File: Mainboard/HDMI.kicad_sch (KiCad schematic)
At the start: 54 parts, among them J3 HDMI_A, Q1 2N7002, Q2 2SK3018, Q3 2SK3018, Q4 2SK3018, U1 TPAZ1023-04F, U2 TPAZ1023-04F, U6 ADV7613WBBCZ, Y1 SiT8008xx-1x-xxE

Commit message: Added HDMI > LDVS screens
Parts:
- removed C25: 100nF/16V, A_HDJ_Library:C_0402_1005Metric, symbol Device:C
- removed F1: 6V/50mA, A_HDJ_Library:R_0603_1608Metric, symbol Device:Fuse
- removed J3: HDMI_A, A_HDJ_Library:HDMI_A_Molex_208658-1001_Horizontal, symbol Connector:HDMI_A
- renumbered C17 to C25, C18 to C33, C19 to C34, C20 to C35, C21 to C36, C22 to C37, C23 to C38, C24 to C39, D1 to D34, D2 to D35, D3 to D36, D4 to D37, Q2 to Q10, Q3 to Q17, Q4 to Q18, Q1 to Q9, R5 to R104, R6 to R105, R7 to R106, R8 to R107, R9 to R108, R10 to R109, R11 to R110, R12 to R111, R13 to R112, R14 to R113, R15 to R114, R16 to R115, R17 to R116, R18 to R117, R19 to R118, R20 to R119, R21 to R120, R22 to R121, R23 to R122, R24 to R123, R25 to R124, R61 to R125, R62 to R126, R98 to R127, R99 to R128, R100 to R129, R101 to R130, R102 to R131, R103 to R132, R3 to R28, R4 to R76, U6 to U20, U1 to U7, U2 to U8, Y1 to Y2
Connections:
- net +1V8: now also U20.B7 (INT), U20.C3 (CVDD), U20.C6 (DVDD), U20.D3 (CVDD), U20.D6 (DVDD), U20.E3 (CVDD), U20.E6 (DVDD), U20.E7 (DVDD), U20.G1 (CVDD), U20.G2 (CVDD), U20.H2 (LTX_VDD), U20.H3 (LTX_VDD), U20.H6 (LTX_VDD), U20.H7 (LTX_VDD)
- net +3V3: now also U20.F3 (TVDD), U20.F7 (DVDDIO), U20.G3 (TVDD), U20.G7 (DVDDIO)
- net +5V: now also U20.B1 (RXA_5V)
- net DDC_SCL: now also U20.A3 (DDCA_SCL)
- net DDC_SDA: now also U20.A2 (DDCA_SDA)
- net GND: now also U20.A7 (RESET*), U20.B6 (CS*)
- net HPD: now also U20.B2 (HPA_A)
- net TMDS_CK+: now also U20.C1 (RXA_C+)
- net TMDS_CK-: now also U20.C2 (RXA_C-)
- net TMDS_D0+: now also U20.D1 (RXA_0+)
- net TMDS_D0-: now also U20.D2 (RXA_0-)
- net TMDS_D1+: now also U20.E1 (RXA_1+)
- net TMDS_D1-: now also U20.E2 (RXA_1-)
- net TMDS_D2+: now also U20.F1 (RXA_2+)
- net TMDS_D2-: now also U20.F2 (RXA_2-)
- net I2C2_SCL: now reaches U20.A8 (SCL)
- net I2C2_SDA: now reaches U20.B8 (SDA)
- net LTX2_3-: now reaches U20.H1 (LTX2_3-)
- net LTX1_0-: now reaches U20.H10 (LTX1_0-)
- net LTX2_3+: now reaches U20.J1 (LTX2_3+)
- net LTX1_0+: now reaches U20.J10 (LTX1_0+)
- net LTX2_C-: now reaches U20.J2 (LTX2_C-)
- net LTX2_2-: now reaches U20.J3 (LTX2_2-)
- net LTX2_1-: now reaches U20.J4 (LTX2_1-)
- net LTX2_0-: now reaches U20.J5 (LTX2_0-)
- net LTX1_3-: now reaches U20.J6 (LTX1_3-)
- net LTX1_C-: now reaches U20.J7 (LTX1_C-)
- net LTX1_2-: now reaches U20.J8 (LTX1_2-)
- net LTX1_1-: now reaches U20.J9 (LTX1_1-)
- net LTX2_C+: now reaches U20.K2 (LTX2_C+)
- net LTX2_2+: now reaches U20.K3 (LTX2_2+)
- net LTX2_1+: now reaches U20.K4 (LTX2_1+)
- net LTX2_0+: now reaches U20.K5 (LTX2_0+)
- net LTX1_3+: now reaches U20.K6 (LTX1_3+)
- net LTX1_C+: now reaches U20.K7 (LTX1_C+)
- net LTX1_2+: now reaches U20.K8 (LTX1_2+)
- net LTX1_1+: now reaches U20.K9 (LTX1_1+)
- net DDI_B_DDC_SCL renamed TCP_0_DDC_SCL
- net TCP_0_DDC_SCL: no longer U20.A3 (DDCA_SCL)
- net DDI_B_DDC_SDA renamed TCP_0_DDC_SDA
- net TCP_0_DDC_SDA: no longer U20.A2 (DDCA_SDA)
- net DDI_B_HPD renamed TCP_0_HPD
- net TCP_0_HPD: no longer U20.B2 (HPA_A)
- net DDI_B_TX0+ renamed TCP_0_TX0+
- net DDI_B_TX0- renamed TCP_0_TX0-
- net DDI_B_TX1+ renamed TCP_0_TX1+
- net DDI_B_TX1- renamed TCP_0_TX1-
- net DDI_B_TX2+ renamed TCP_0_TX2+
- net DDI_B_TX2- renamed TCP_0_TX2-
- net DDI_B_TX3+ renamed TCP_0_TX3+
- net DDI_B_TX3- renamed TCP_0_TX3-
- no-connect marks 3 -> 10
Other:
- moved on the sheet: C25, C33, C34, C35, C36, C37, C38, C39, D34, D35, D36, D37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

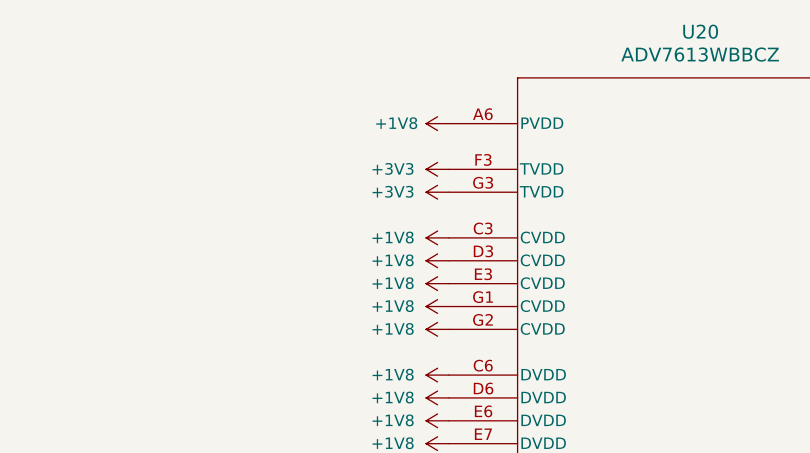
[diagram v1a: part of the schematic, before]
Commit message: Mainboard Progress, Updated CTRL-L for new Joystick Module
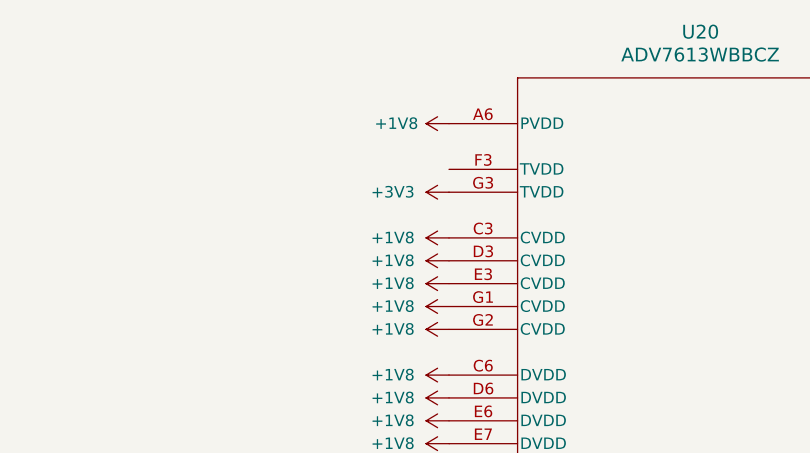
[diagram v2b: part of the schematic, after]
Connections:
- net +3V3: no longer U20.F3 (TVDD)
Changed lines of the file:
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@@
 	)
 	(symbol
-		(lib_name "+5V_1")
-		(lib_id "power:+5V")
-		(at 411.48 212.09 90)
-		(unit 1)
-		(body_style 1)
-		(exclude_from_sim no)
-		(in_bom yes)
-		(on_board yes)
-		(in_pos_files yes)
-		(dnp no)
-		(fields_autoplaced yes)
-		(property "Reference" "#PWR0169"
-			(at 415.29 212.09 0)
-			(hide yes)
-			(show_name no)
-			(do_not_autoplace no)
-			(effects
-				(font
-					(size 1.27 1.27)
-				)
-			)
-		)
-		(property "Value" "+5V"
-			(at 407.67 212.0899 90)
-			(show_name no)
-			(do_not_autoplace no)
-			(effects
-				(font
-					(size 1.27 1.27)
-				)
-				(justify left)
-			)
-		)
-		(property "Footprint" ""
-			(at 411.48 212.09 0)
-			(hide yes)
-			(show_name no)
-			(do_not_autoplace no)
-			(effects
-				(font
-					(size 1.27 1.27)
-				)
-			)
-		)
-		(property "Datasheet" ""
-			(at 411.48 212.09 0)
-			(hide yes)
-			(show_name no)
-			(do_not_autoplace no)
-			(effects
-				(font
-					(size 1.27 1.27)
-				)
-			)
-		)
-		(property "Description" "Power symbol creates a global label with name \"+5V\""
-			(at 411.48 212.09 0)
-			(hide yes)
-			(show_name no)
-			(do_not_autoplace no)
-			(effects
-				(font
-					(size 1.27 1.27)
-				)
-			)
-		)
-		(pin "1"
-		)
-		(instances
-			(project "[DFR1142]Lite Carrier for LattePanda Mu(V2)"
-				(path "/2a6d114a-7fd7-4207-b5f7-4ea9c34f36aa/18101890-54d7-4e46-b21c-77a03deab3c0"
-					(reference "#PWR0169")
-					(unit 1)
-				)
-				(path "/2a6d114a-7fd7-4207-b5f7-4ea9c34f36aa/b169c362-0273-44a3-bb19-0bcbad977976"
-					(reference "#PWR0169")
-					(unit 1)
-				)
-			)
-		)
-	)
-	(symbol
 		(lib_id "Device:R")
 		(at 248.92 350.52 90)
@@
 	)
 	(symbol
-		(lib_name "+3V3_1")
-		(lib_id "power:+3V3")
-		(at 411.48 74.93 90)
+		(lib_id "Oscillator:SiT8008xx-1x-xxE")
+		(at 497.84 179.07 180)
 		(unit 1)
 		(body_style 1)
@@
 		(dnp no)
 		(fields_autoplaced yes)
-		(property "Reference" "#PWR0152"
-			(at 415.29 74.93 0)
-			(hide yes)
+		(property "Reference" "Y2"
+			(at 513.08 173.6246 0)
 			(show_name no)
 			(do_not_autoplace no)
@@
 			)
 		)
-		(property "Value" "+3V3"
-			(at 407.67 74.9299 90)
+		(property "Value" "SiT8008xx-1x-xxE"
+			(at 513.08 176.1646 0)
 			(show_name no)
 			(do_not_autoplace no)
@@
 					(size 1.27 1.27)
 				)
-				(justify left)
 			)
 		)
-		(property "Footprint" ""
-			(at 411.48 74.93 0)
+		(property "Footprint" "Oscillator:Oscillator_SMD_SiT_PQFN-4Pin_2.5x2.0mm"
+			(at 497.84 179.07 0)
 			(hide yes)
 			(show_name no)
@@
 			)
 		)
-		(property "Datasheet" ""
-			(at 411.48 74.93 0)
+		(property "Datasheet" "https://www.sitime.com/support/resource-library/datasheets/sit8008-datasheet"
+			(at 497.84 179.07 0)
 			(hide yes)
 			(show_name no)
@@
 			)
 		)
-		(property "Description" "Power symbol creates a global label with name \"+3V3\""
-			(at 411.48 74.93 0)
+		(property "Description" "SiTime Low Power Mems programmable oscillator, 1MHz to 110MHz, PQFN-4, 2.5x2.0mm (with output enable pin)"
+			(at 497.84 179.07 0)
 			(hide yes)
 			(show_name no)
@@
 			)
 		)
+		(pin "3"
+		)
 		(pin "1"
 		)
+		(pin "2"
+		)
+		(pin "4"
+		)
 		(instances
 			(project "[DFR1142]Lite Carrier for LattePanda Mu(V2)"
 				(path "/2a6d114a-7fd7-4207-b5f7-4ea9c34f36aa/18101890-54d7-4e46-b21c-77a03deab3c0"
-					(reference "#PWR0152")
+					(reference "Y2")
 					(unit 1)
 				)
 				(path "/2a6d114a-7fd7-4207-b5f7-4ea9c34f36aa/b169c362-0273-44a3-bb19-0bcbad977976"
-					(reference "#PWR0152")
+					(reference "Y1")
 					(unit 1)
 				)
@@
 	)
 	(symbol
-		(lib_id "Oscillator:SiT8008xx-1x-xxE")
-		(at 497.84 179.07 180)
+		(lib_id "Device:R")
+		(at 474.98 156.21 90)
 		(unit 1)
 		(body_style 1)
@@
 		(in_pos_files yes)
 		(dnp no)
-		(fields_autoplaced yes)
-		(property "Reference" "Y2"
-			(at 513.08 173.6246 0)
+		(property "Reference" "R130"
+			(at 474.98 149.86 90)
+			(hide yes)
 			(show_name no)
 			(do_not_autoplace no)
@@
 			)
 		)
-		(property "Value" "SiT8008xx-1x-xxE"
-			(at 513.08 176.1646 0)
+		(property "Value" "1k"
+			(at 481.076 156.21 90)
 			(show_name no)
 			(do_not_autoplace no)
@@
 			)
 		)
-		(property "Footprint" "Oscillator:Oscillator_SMD_SiT_PQFN-4Pin_2.5x2.0mm"
-			(at 497.84 179.07 0)
+		(property "Footprint" ""
+			(at 474.98 157.988 90)
 			(hide yes)
 			(show_name no)
@@
 			)
 		)
-		(property "Datasheet" "https://www.sitime.com/support/resource-library/datasheets/sit8008-datasheet"
-			(at 497.84 179.07 0)
+		(property "Datasheet" ""
+			(at 474.98 156.21 0)
 			(hide yes)
 			(show_name no)
@@
 			)
 		)
-		(property "Description" "SiTime Low Power Mems programmable oscillator, 1MHz to 110MHz, PQFN-4, 2.5x2.0mm (with output enable pin)"
-			(at 497.84 179.07 0)
+		(property "Description" "Resistor"
+			(at 474.98 156.21 0)
 			(hide yes)
 			(show_name no)
@@
 			)
 		)
-		(pin "3"
-		)
 		(pin "1"
 		)
 		(pin "2"
 		)
-		(pin "4"
-		)
 		(instances
 			(project "[DFR1142]Lite Carrier for LattePanda Mu(V2)"
 				(path "/2a6d114a-7fd7-4207-b5f7-4ea9c34f36aa/18101890-54d7-4e46-b21c-77a03deab3c0"
-					(reference "Y2")
+					(reference "R130")
 					(unit 1)
 				)
 				(path "/2a6d114a-7fd7-4207-b5f7-4ea9c34f36aa/b169c362-0273-44a3-bb19-0bcbad977976"
-					(reference "Y1")
+					(reference "R101")
 					(unit 1)
 				)
@@
 	)
 	(symbol
-		(lib_id "Device:R")
-		(at 474.98 156.21 90)
+		(lib_name "+5V_1")
+		(lib_id "power:+5V")
+		(at 411.48 212.09 90)
 		(unit 1)
 		(body_style 1)
@@
 		(in_pos_files yes)
 		(dnp no)
-		(property "Reference" "R130"
-			(at 474.98 149.86 90)
+		(fields_autoplaced yes)
+		(property "Reference" "#PWR0152"
+			(at 415.29 212.09 0)
 			(hide yes)
 			(show_name no)
@@
 			)
 		)
-		(property "Value" "1k"
-			(at 481.076 156.21 90)
+		(property "Value" "+5V"
+			(at 407.67 212.0899 90)
 			(show_name no)
 			(do_not_autoplace no)
@@
 					(size 1.27 1.27)
 				)
+				(justify left)
 			)
 		)
 		(property "Footprint" ""
-			(at 474.98 157.988 90)
+			(at 411.48 212.09 0)
 			(hide yes)
 			(show_name no)
@@
 		)
 		(property "Datasheet" ""
-			(at 474.98 156.21 0)
+			(at 411.48 212.09 0)
 			(hide yes)
 			(show_name no)
@@
 			)
 		)
-		(property "Description" "Resistor"
-			(at 474.98 156.21 0)
+		(property "Description" "Power symbol creates a global label with name \"+5V\""
+			(at 411.48 212.09 0)
 			(hide yes)
 			(show_name no)
@@
 		(pin "1"
 		)
-		(pin "2"
-		)
 		(instances
 			(project "[DFR1142]Lite Carrier for LattePanda Mu(V2)"
 				(path "/2a6d114a-7fd7-4207-b5f7-4ea9c34f36aa/18101890-54d7-4e46-b21c-77a03deab3c0"
-					(reference "R130")
+					(reference "#PWR0152")
 					(unit 1)
 				)
 				(path "/2a6d114a-7fd7-4207-b5f7-4ea9c34f36aa/b169c362-0273-44a3-bb19-0bcbad977976"
-					(reference "R101")
+					(reference "#PWR0169")
 					(unit 1)
 				)
